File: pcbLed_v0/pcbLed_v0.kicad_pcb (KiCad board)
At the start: 2 copper layers, 102.9 x 59.7 mm, 20 parts, among them IC1 SN74AHCT125N, J1 Screw_Terminal_01x02, J2 Conn_01x02_Male, J3 Conn_01x03_Male, J4 Screw_Terminal_01x04, J6 Conn_01x03_Male, U1 WeMos_D1_mini, U2 DS18B20

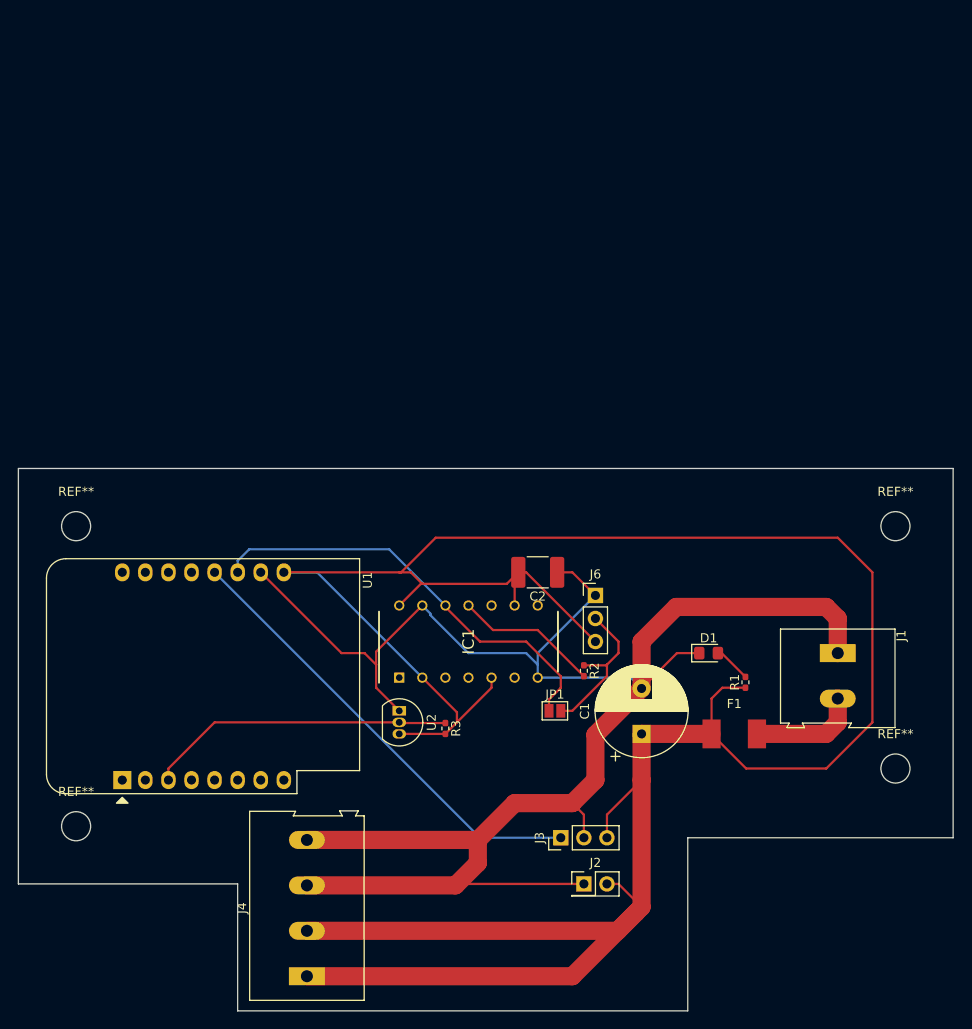
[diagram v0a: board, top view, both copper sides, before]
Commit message: split to 2 pcbs; one for power supply; one for the other
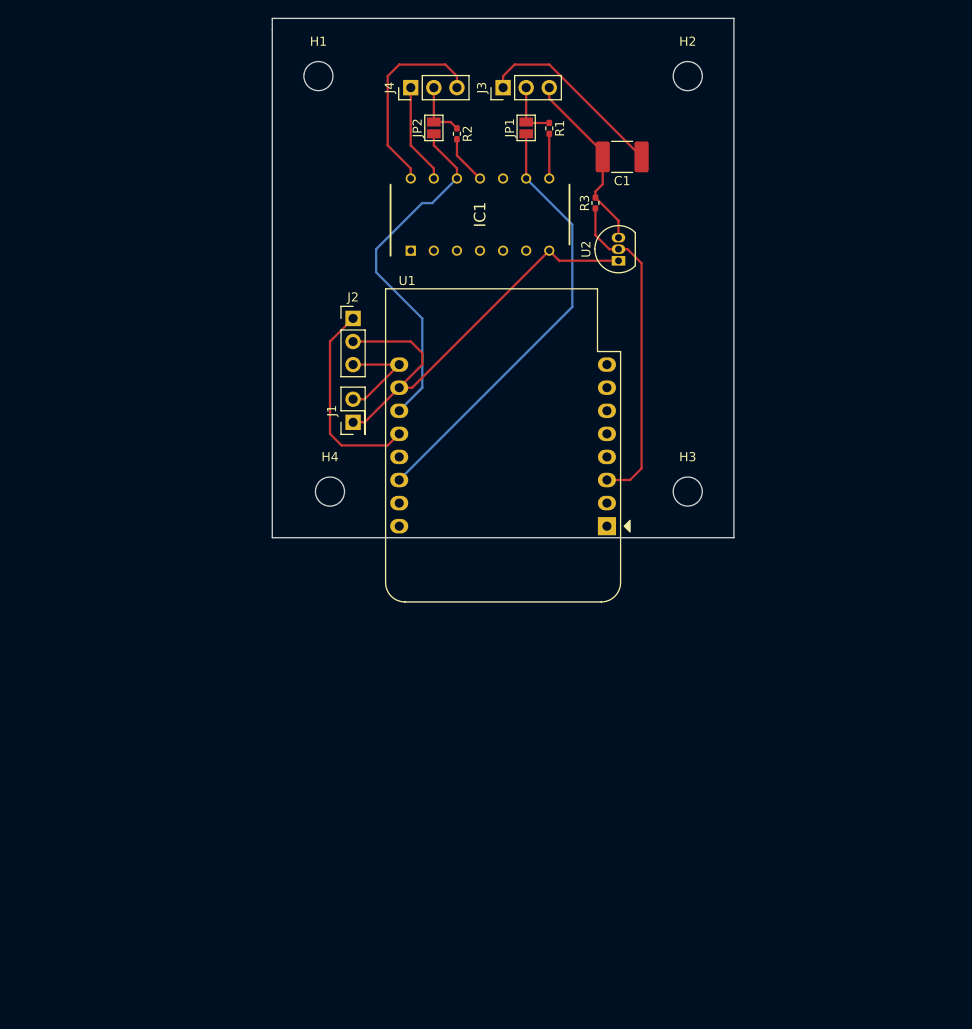
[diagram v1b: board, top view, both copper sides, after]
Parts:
- removed the C1 at (115.6, 111.8)
- removed D1: LED EVL 17-21/GHC-X, LED_SMD:LED_0805_2012Metric_Pad1.15x1.40mm_HandSolder
- removed F1: Fuse 10A, Belfuse220043:BELFUSE220043_10A_SMD2410
- removed J6: Conn_01x03_Male, Connector_PinHeader_2.54mm:PinHeader_1x03_P2.54mm_Vertical
- removed REF** (x4): MountingHole_3.2mm_M3_DIN965, MountingHole:MountingHole_3.2mm_M3_DIN965
- added H1: MountingHole, MountingHole:MountingHole_3.2mm_M3_DIN965, F.Cu at (80.0, 39.4)
- added H2: MountingHole, MountingHole:MountingHole_3.2mm_M3_DIN965, F.Cu at (120.7, 39.4)
- added H3: MountingHole, MountingHole:MountingHole_3.2mm_M3_DIN965, F.Cu at (120.7, 85.1)
- added H4: MountingHole, MountingHole:MountingHole_3.2mm_M3_DIN965, F.Cu at (81.3, 85.1)
- added JP1: SolderJumper_2_Open, Jumper:SolderJumper-2_P1.3mm_Open_Pad1.0x1.5mm, F.Cu at (102.9, 45.1)
- J1: value Screw_Terminal_01x02 -> Conn_01x02_Male; footprint TerminalBlock:TerminalBlock_Altech_AK300-2_P5.00mm -> Connector_PinHeader_2.54mm:PinHeader_2x01_P2.54mm_Vertical
- J2: value Conn_01x02_Male -> Conn_01x03_Male; footprint Connector_PinHeader_2.54mm:PinHeader_2x01_P2.54mm_Vertical -> Connector_PinHeader_2.54mm:PinHeader_1x03_P2.54mm_Vertical
- J4: value Screw_Terminal_01x04 -> Conn_01x03_Male; footprint TerminalBlock:TerminalBlock_Altech_AK300-4_P5.00mm -> Connector_PinHeader_2.54mm:PinHeader_1x03_P2.54mm_Vertical
- R1: value 100 RND 0402 1 100 -> 470R
- moved J4 98.5 mm to (90.2, 40.6)
- moved J3 82.8 mm to (100.3, 40.6)
- moved J2 67.2 mm to (83.8, 66.0)
- moved JP2 65.5 mm to (92.7, 45.1), turned to 90 degrees
- moved R1 64.7 mm to (105.4, 45.1), turned to 270 degrees
- moved R2 60.7 mm to (95.2, 45.7)
- moved U1 60.2 mm to (111.8, 88.9), turned to 180 degrees
- moved R3 60.1 mm to (110.5, 53.3), turned to 90 degrees
- moved J1 59.1 mm to (83.8, 77.5), turned to 90 degrees
- moved U2 55.1 mm to (113.0, 59.7), turned to 90 degrees
- moved IC1 47.0 mm to (97.8, 54.6)
- moved C1 46.7 mm to (113.4, 48.3)
- renumbered C2 to C1, JP1 to JP2
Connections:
- IC1 pad 9: +5V -> D1
- J1 pad 2: Net-(F1-Pad2) -> +5V
- J2 pad 1: GND -> Net-(J2-Pad1)
- J2 pad 2: +5V -> GND
- J3 pad 1: Net-(J3-Pad1) -> GND
- J3 pad 2: GND -> Net-(J3-Pad2)
- J4 pad 1: +5V -> GND
- J4 pad 2: +5V -> Net-(J4-Pad2)
- J4 pad 3: GND -> +5V
- JP2 pad 2: Net-(J6-Pad2) -> Net-(J4-Pad2)
- R1 pad 1: +5V -> Net-(J3-Pad2)
- R1 pad 2: Net-(D1-Pad2) -> Net-(IC1-Pad8)
- R2 pad 1: Net-(J6-Pad2) -> Net-(J4-Pad2)
- U1 pad 12: Net-(J3-Pad1) -> Net-(J2-Pad1)
- U1 pad 14: Net-(U1-Pad14) -> D1
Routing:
- net +5V: track 303.5 -> 54.3 mm
- net GND: track 204.2 -> 82.8 mm
- net Net-(J3-Pad1): track 50.2 -> 0.00 mm
- net D1: track 0.00 -> 48.1 mm
- net Net-(J2-Pad1): track 0.00 -> 22.4 mm
- net Net-(J6-Pad2): track 17.2 -> 0.00 mm
- net Net-(F1-Pad2): track 12.0 -> 0.00 mm
- net Net-(IC1-Pad11): track 15.9 -> 5.37 mm
- net Net-(IC1-Pad12): track 47.6 -> 39.0 mm
- net Net-(J4-Pad2): track 0.00 -> 6.61 mm
- net Net-(J3-Pad2): track 0.00 -> 6.36 mm
- net Net-(IC1-Pad8): track 0.00 -> 4.92 mm
- net Net-(D1-Pad2): track 4.11 -> 0.00 mm
- net Net-(R3-Pad1): track 33.9 -> 36.2 mm
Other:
- board size 102.9 x 59.7 mm -> 50.8 x 57.1 mm
